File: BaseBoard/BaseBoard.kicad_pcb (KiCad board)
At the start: 2 copper layers, 100 x 56 mm, 38 parts, among them J1 Raspberry_Pi_2_3, J10 Conn_01x01, J11 Conn_01x01, J12 Conn_01x02_Female, J13 Conn_01x02_Female, J14 Conn_01x02_Female, J15 Conn_01x02_Female, J16 Conn_01x02_Female, J17 MOTOR, J18 MOTOR, J19 MOTOR, J2 Longan_A, J20 MOTOR, J21 Conn_01x01, J22 Conn_01x01, J3 TB6612_A, J4 TB6612_A, J5 Longan_C, J6 Longan_B, J7 TB6612_B, J8 TB6612_B, J9 Conn_02x04, U1 SY6912

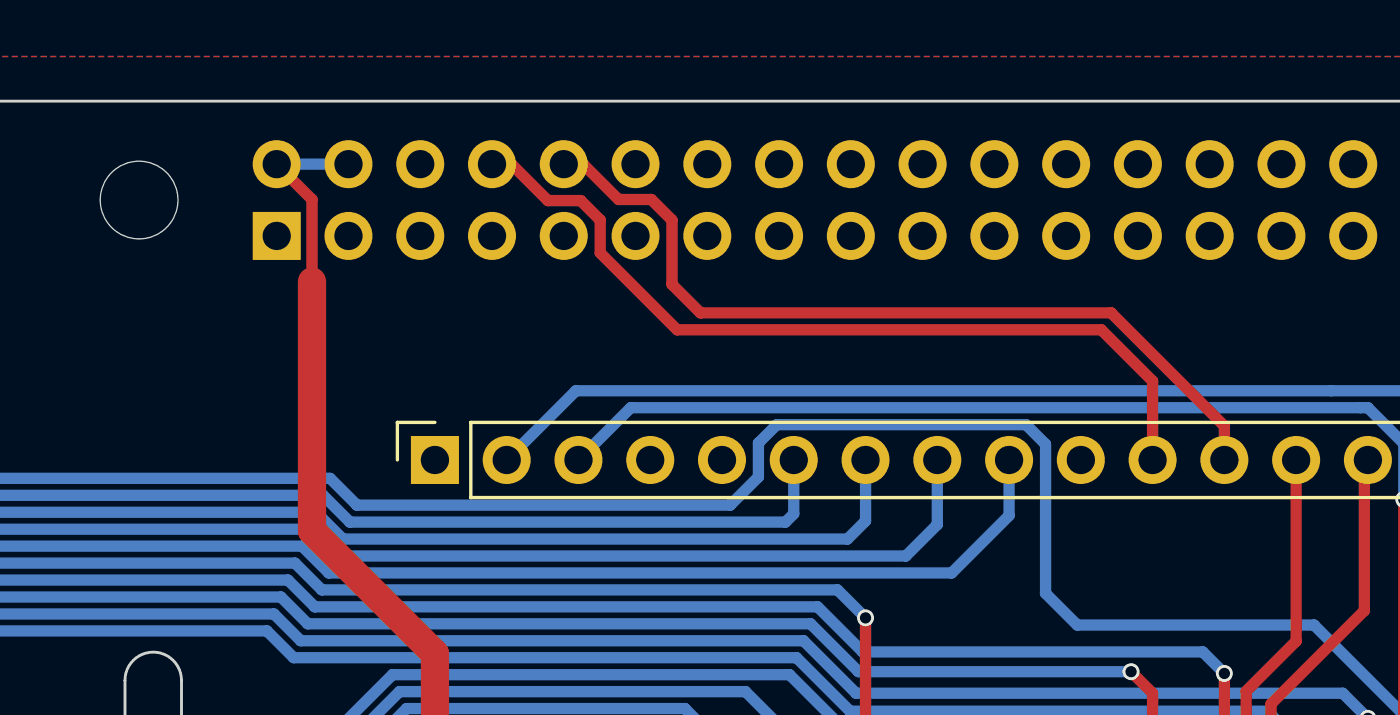
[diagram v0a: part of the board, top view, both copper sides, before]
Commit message: 添加BOM，板子上添加IMU接口
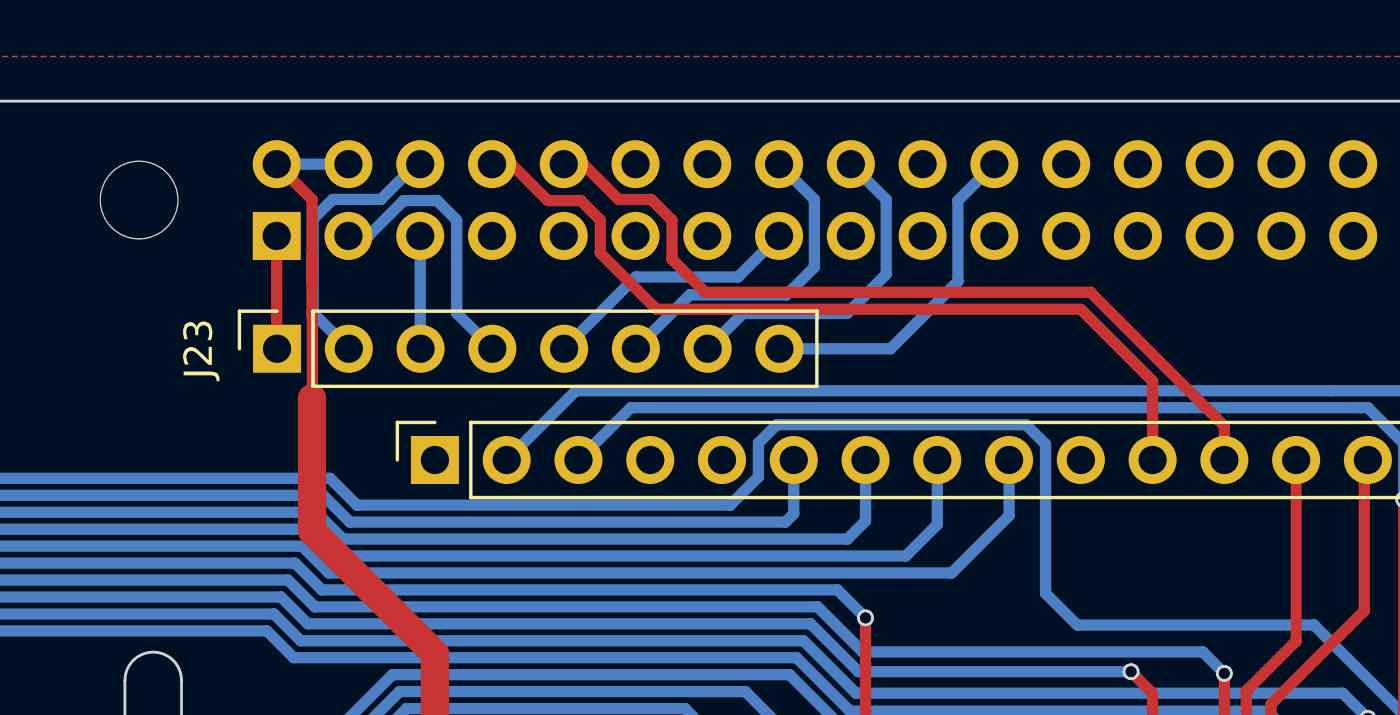
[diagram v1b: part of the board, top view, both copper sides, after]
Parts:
- added J23: IMU, Connector_PinSocket_2.54mm:PinSocket_1x08_P2.54mm_Vertical, F.Cu at (118.9, 57.4)
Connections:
- J1 pad 15: Net-(J1-Pad15) -> /GPIO22
- J1 pad 16: Net-(J1-Pad16) -> /GPIO23
- J1 pad 18: Net-(J1-Pad18) -> /GPIO24
- J1 pad 22: Net-(J1-Pad22) -> /GPIO25
- J1 pad 3: Net-(J1-Pad3) -> /SDA
- J1 pad 5: Net-(J1-Pad5) -> /SCL
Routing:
- net /GPIO25: track 0.00 -> 12.0 mm
- net /GPIO24: track 0.00 -> 11.8 mm
- net /GPIO23: track 0.00 -> 11.7 mm
- net /SDA: track 0.00 -> 9.71 mm
- net GND: track 132.6 -> 142.4 mm
- net /GPIO22: track 0.00 -> 9.26 mm
- net /SCL: track 0.00 -> 4.00 mm
- net +3.3VA: track 0.00 -> 4.00 mm
- net +5V: track 40.9 -> 41.8 mm
- net /CTL_TX: track 29.8 -> 29.2 mm

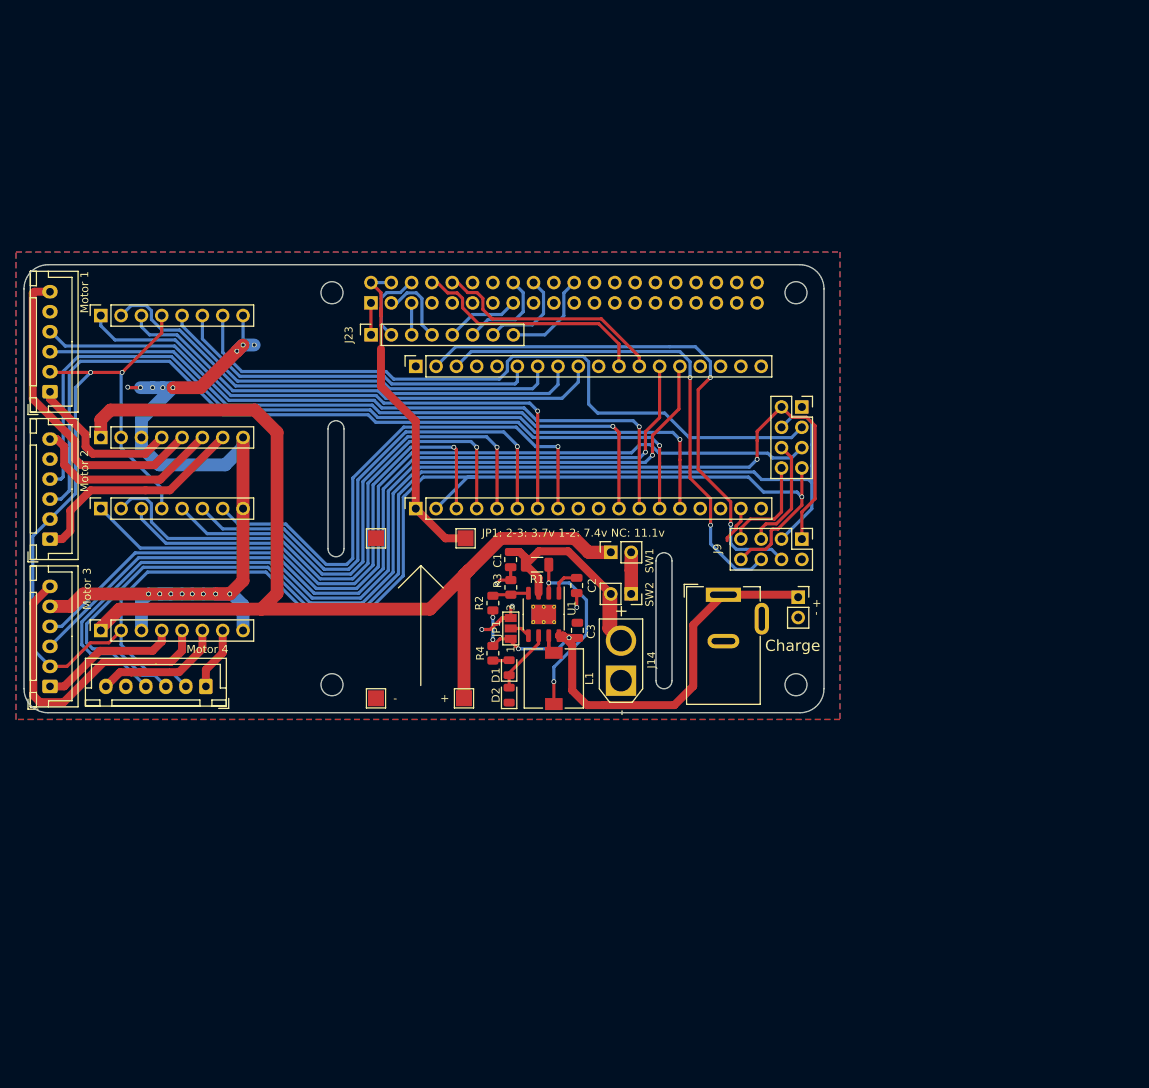
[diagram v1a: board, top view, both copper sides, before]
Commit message: 更新线路板布局
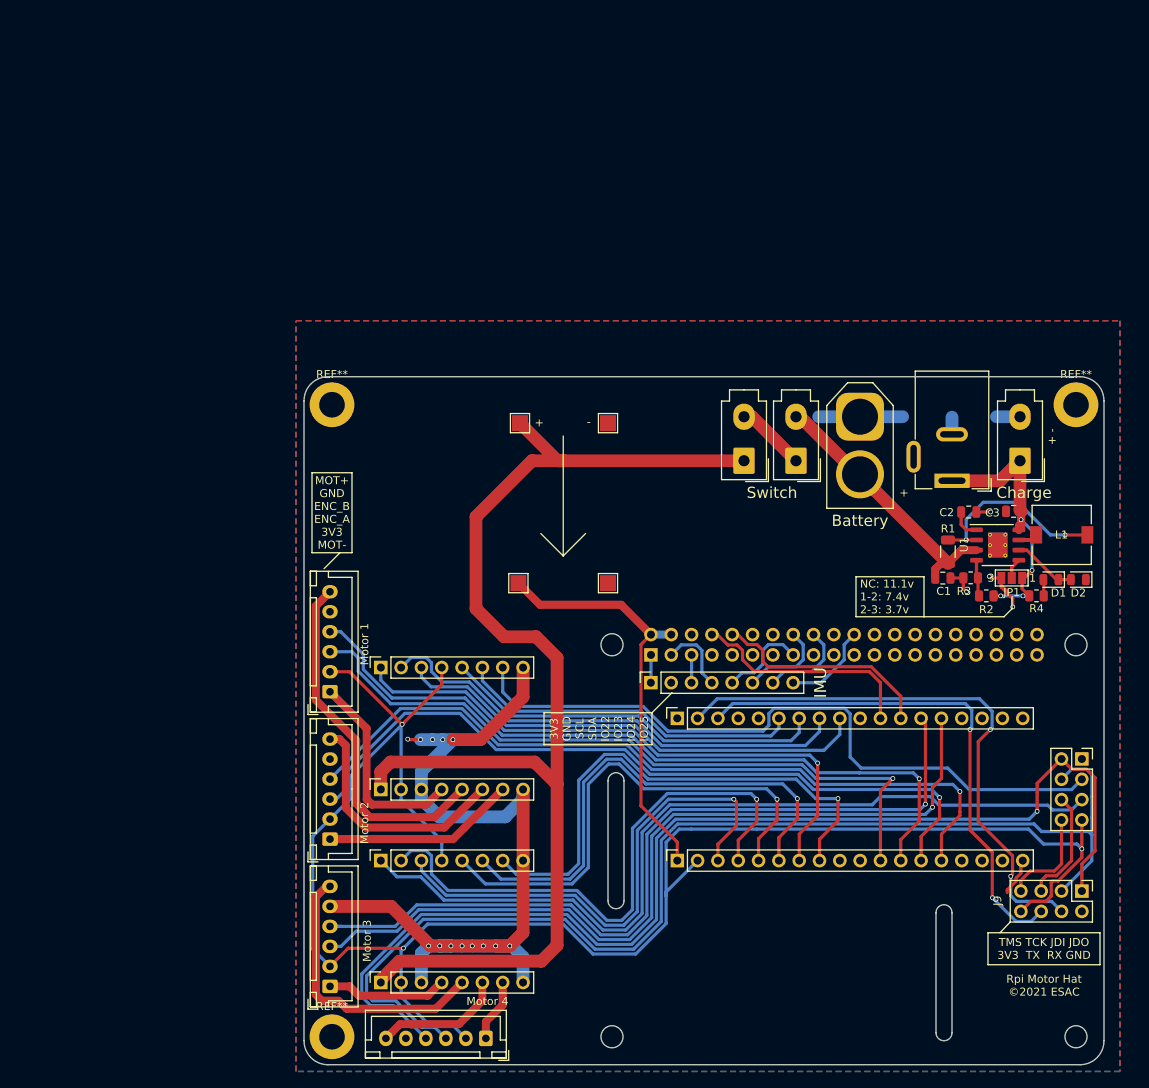
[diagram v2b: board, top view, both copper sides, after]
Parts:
- added REF**: MountingHole_3.2mm_M3_DIN965_Pad, MountingHole:MountingHole_3.2mm_M3_DIN965_Pad, F.Cu at (114.0, 145.1)
- added REF**: MountingHole_3.2mm_M3_DIN965_Pad, MountingHole:MountingHole_3.2mm_M3_DIN965_Pad, F.Cu at (114.0, 66.1)
- added REF**: MountingHole_3.2mm_M3_DIN965_Pad, MountingHole:MountingHole_3.2mm_M3_DIN965_Pad, F.Cu at (207.0, 66.1)
- J12, J13, J16: footprint Connector_PinSocket_2.54mm:PinSocket_1x02_P2.54mm_Vertical -> Connector_Molex:Molex_Mini-Fit_Jr_5566-02A_2x01_P4.20mm_Vertical
- J14: footprint Connector_AMASS:AMASS_XT30U-M_1x02_P5.0mm_Vertical -> Connector_AMASS:AMASS_XT60-M_1x02_P7.20mm_Vertical
- moved D2 72.6 mm to (207.3, 88.0), turned to 180 degrees
- moved D1 68.6 mm to (203.9, 88.0), turned to 180 degrees
- moved R4 68.3 mm to (202.1, 90.0), turned to 0 degrees
- moved L1 66.0 mm to (205.2, 82.4), turned to 0 degrees
- moved JP1 62.9 mm to (199.0, 87.8), turned to 180 degrees
- moved R2 61.7 mm to (195.8, 90.0), turned to 0 degrees
- moved R3 57.5 mm to (193.8, 87.8), turned to 0 degrees
- moved U1 57.4 mm to (197.2, 83.7), turned to 0 degrees
- moved C3 56.5 mm to (199.2, 79.5), turned to 180 degrees
- moved ? 56.2 mm to (207.0, 145.1)
- moved ? 56.2 mm to (149.0, 145.1)
- moved J1 56.2 mm to (153.9, 97.4)
- moved J4 56.2 mm to (120.1, 138.4)
- moved J7 56.2 mm to (120.1, 99.0)
- moved ? 56.2 mm to (207.0, 96.1)
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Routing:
- net VBUS: track 66.1 -> 35.3 mm
- net +12V: track 137.1 -> 154.0 mm
- net +5V: track 41.8 -> 52.4 mm
- net /ENC2_B: track 105.7 -> 96.3 mm
- net /ENC2_A: track 104.2 -> 95.1 mm
- net /MOT1_N: track 19.4 -> 25.8 mm
- net /MOT2_P: track 24.7 -> 30.2 mm
- net GND: track 142.4 -> 147.2 mm, vias 20 -> 17
- net /ENC1_B: track 88.8 -> 93.6 mm
- net /ENC3_A: track 107.7 -> 103.1 mm
- net /MOT1_P: track 40.3 -> 44.7 mm
- net +3V3: track 229.9 -> 225.7 mm
- net /MOT2_N: track 28.3 -> 24.2 mm
- net /ENC1_A: track 84.8 -> 88.8 mm
- net /MOT3_P: track 38.7 -> 34.9 mm
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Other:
- board size 100 x 56 mm -> 100 x 86 mm
- board text added: "3V3 GND SCL SDA IO22 IO23 IO24 IO25"
- board text added: "Battery"
- board text added: "IMU"
- board text added: "MOT+ GND ENC_B ENC_A 3V3 MOT-"
- board text added: "NC: 11.1v 1-2: 7.4v 2-3: 3.7v"
- board text added: "Rpi Motor Hat ©2021 ESAC"
- board text added: "Switch"
- board text added: "TMS TCK JDI JDO 3V3 TX RX GND"
- board text removed: "JP1: 2-3: 3.7v 1-2: 7.4v NC: 11.1v"
- board text removed: "SW1"
- board text removed: "SW2"

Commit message: 更新线路板设计，添加PD芯片
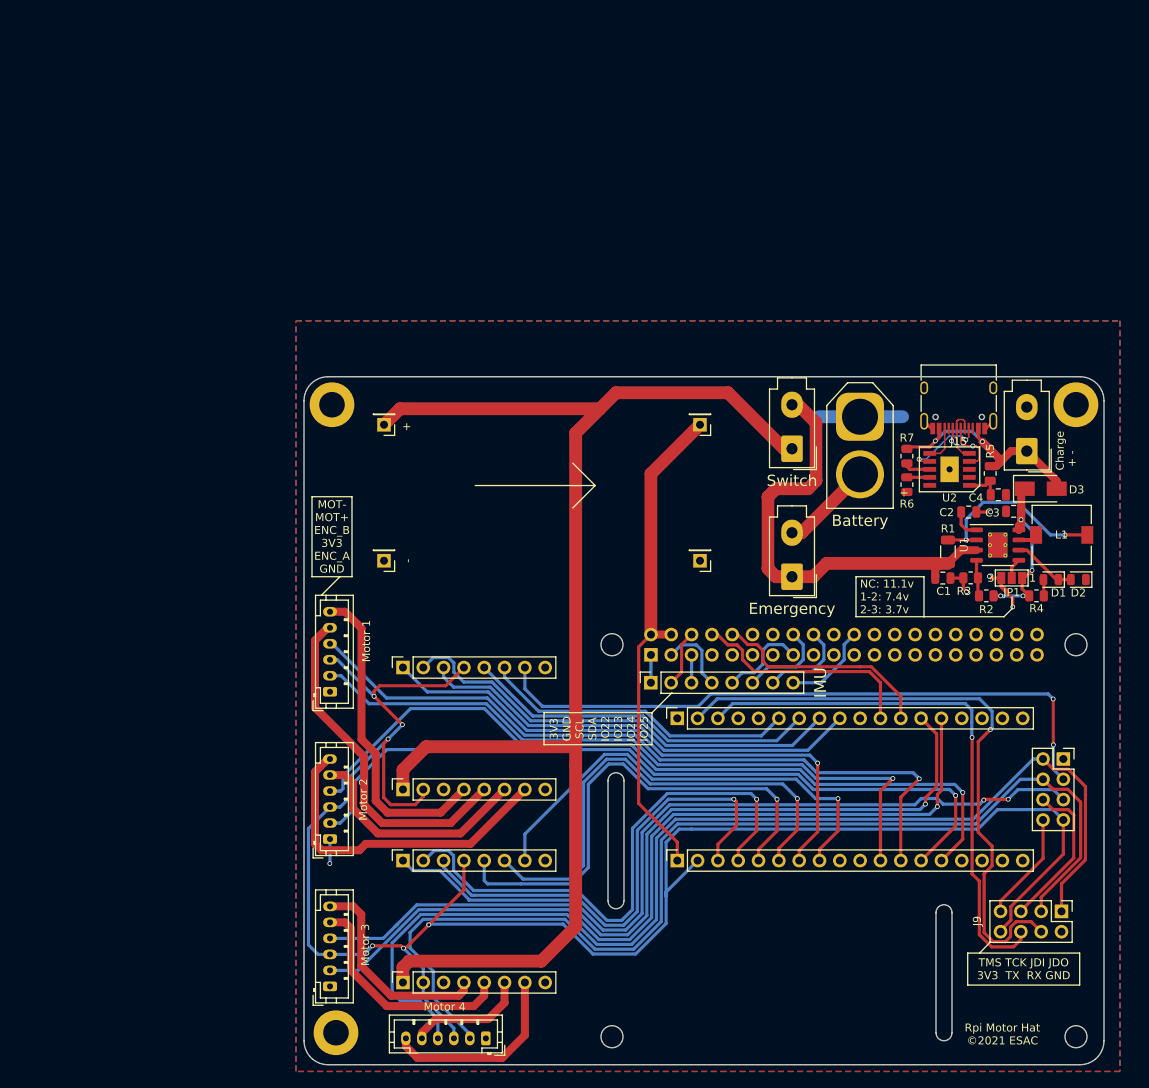
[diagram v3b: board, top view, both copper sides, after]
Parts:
- added C4: 1uF, Capacitor_SMD:C_0805_2012Metric, F.Cu at (197.3, 77.4)
- added D3: SS34, Diode_SMD:D_SMA, F.Cu at (202.6, 76.6)
- added R5: 10k, Resistor_SMD:R_0805_2012Metric, F.Cu at (196.3, 74.7)
- added R6: 56k, Resistor_SMD:R_0805_2012Metric, F.Cu at (185.9, 76.1)
- added R7: 10k, Resistor_SMD:R_0805_2012Metric, F.Cu at (185.9, 72.6)
- added U2: CH224K, Custom:ESSOP10, F.Cu at (191.2, 74.2)
- C3: value 10u/X7R -> 10uF/X7R
- J10, J11, J21, J22: footprint TestPoint:TestPoint_Pad_2.0x2.0mm -> Connector_PinHeader_2.54mm:PinHeader_1x01_P2.54mm_Vertical
- J15: value Conn_01x02_Female -> USB_C_Receptacle_USB2.0; footprint Connector_BarrelJack:BarrelJack_Wuerth_6941xx301002 -> Connector_USB:USB_C_Receptacle_HRO_TYPE-C-31-M-12
- J17, J18, J19, J20: footprint Connector_JST:JST_XH_B6B-XH-A_1x06_P2.50mm_Vertical -> Connector_JST:JST_PH_B6B-PH-K_1x06_P2.00mm_Vertical
- moved J22 28.0 mm to (120.5, 68.6)
- moved J21 24.2 mm to (120.5, 85.6)
- moved J11 22.9 mm to (160.0, 68.6)
- moved J10 22.9 mm to (160.0, 85.6)
- moved J13 14.5 mm to (171.5, 87.6)
- moved J15 10.6 mm to (192.3, 65.1)
- moved J12 6.18 mm to (171.5, 71.6)
- moved J9 3.59 mm to (205.2, 129.5)
- moved J3 2.77 mm to (122.9, 114.2)
- moved J4 2.77 mm to (122.9, 138.4)
- moved J7 2.77 mm to (122.9, 99.0)
- moved J8 2.77 mm to (122.9, 123.1)
- moved J5 2.31 mm to (205.4, 110.4)
- moved J16 1.48 mm to (200.8, 71.9)
- moved REF** 0.71 mm to (114.5, 144.6)
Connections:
- C1 pad 1: /VBAT -> /VBCHG
- C3 pad 1: VBUS -> /VCHARGE
- J10 pad 1: +5V -> GND
- J11 pad 1: GND -> +5V
- J12 pad 2: Net-(J12-Pad2) -> /VBCHG
- J13 pad 1: Net-(J12-Pad2) -> /VBCHG
- J17 pad 1: /MOT1_N -> GND
- J17 pad 2: +3V3 -> /ENC1_A
- J17 pad 3: /ENC1_A -> +3V3
- J17 pad 5: GND -> /MOT1_P
- J17 pad 6: /MOT1_P -> /MOT1_N
- J18 pad 1: /MOT2_N -> GND
- J18 pad 2: +3V3 -> /ENC2_A
- J18 pad 3: /ENC2_A -> +3V3
- J18 pad 5: GND -> /MOT2_P
- J18 pad 6: /MOT2_P -> /MOT2_N
- J19 pad 1: /MOT3_N -> GND
- J19 pad 2: +3V3 -> /ENC3_A
- J19 pad 3: /ENC3_A -> +3V3
- J19 pad 5: GND -> /MOT3_P
- J19 pad 6: /MOT3_P -> /MOT3_N
- J20 pad 1: /MOT4_N -> GND
- J20 pad 2: +3V3 -> /ENC4_A
- J20 pad 3: /ENC4_A -> +3V3
- J20 pad 5: GND -> /MOT4_P
- J20 pad 6: /MOT4_P -> /MOT4_N
- J21 pad 1: +12V -> GND
- J22 pad 1: GND -> +12V
- JP1 pad 1: VBUS -> /VCHARGE
- R1 pad 2: /VBAT -> /VBCHG
- R2 pad 2: VBUS -> /VCHARGE
- R4 pad 1: VBUS -> /VCHARGE
- U1 pad 3: /VBAT -> /VBCHG
- U1 pad 8: VBUS -> /VCHARGE
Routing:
- net GND: track 147.2 -> 36.7 mm, vias 17 -> 5
- net /VBCHG: track 0.00 -> 57.9 mm
- net /VCHARGE: track 0.00 -> 22.4 mm, vias 0 -> 4
- net /VBAT: track 31.7 -> 11.7 mm
- net +12V: track 154.0 -> 172.4 mm
- net /MOT2_N: track 24.2 -> 41.2 mm
- net /MOT4_N: track 7.86 -> 24.2 mm
- net /MOT1_N: track 25.8 -> 39.9 mm
- net /DP: track 0.00 -> 11.6 mm, vias 0 -> 2
- net /CC1: track 0.00 -> 11.3 mm, vias 0 -> 2
- net /MOT3_N: track 15.1 -> 26.4 mm
- net +5V: track 52.4 -> 62.2 mm
- net /ENC4_A: track 143.4 -> 134.0 mm
- net Net-(J12-Pad2): track 8.78 -> 0.00 mm
- net /PWM4: track 65.9 -> 57.6 mm
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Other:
- board text added: "Emergency"
- board text added: "MOT- MOT+ ENC_B 3V3 ENC_A GND"
- board text removed: "MOT+ GND ENC_B ENC_A 3V3 MOT-"
